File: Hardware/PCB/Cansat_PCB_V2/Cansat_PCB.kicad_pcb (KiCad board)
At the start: 6 copper layers, 31.8 x 25.4 mm, 84 parts, among them IC1 Alim STM Baro GPS IMU, IC2 Alim LoRa, J1 Lecteur SD, J2 Connecteur Batterie, J3 Connecteur STLINK, J4 Connecteur Moteur, J5 Connecteur TOF, J6 Connecteur GPS, J7 Connecteur LoRa, J9 Connecteur IHM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

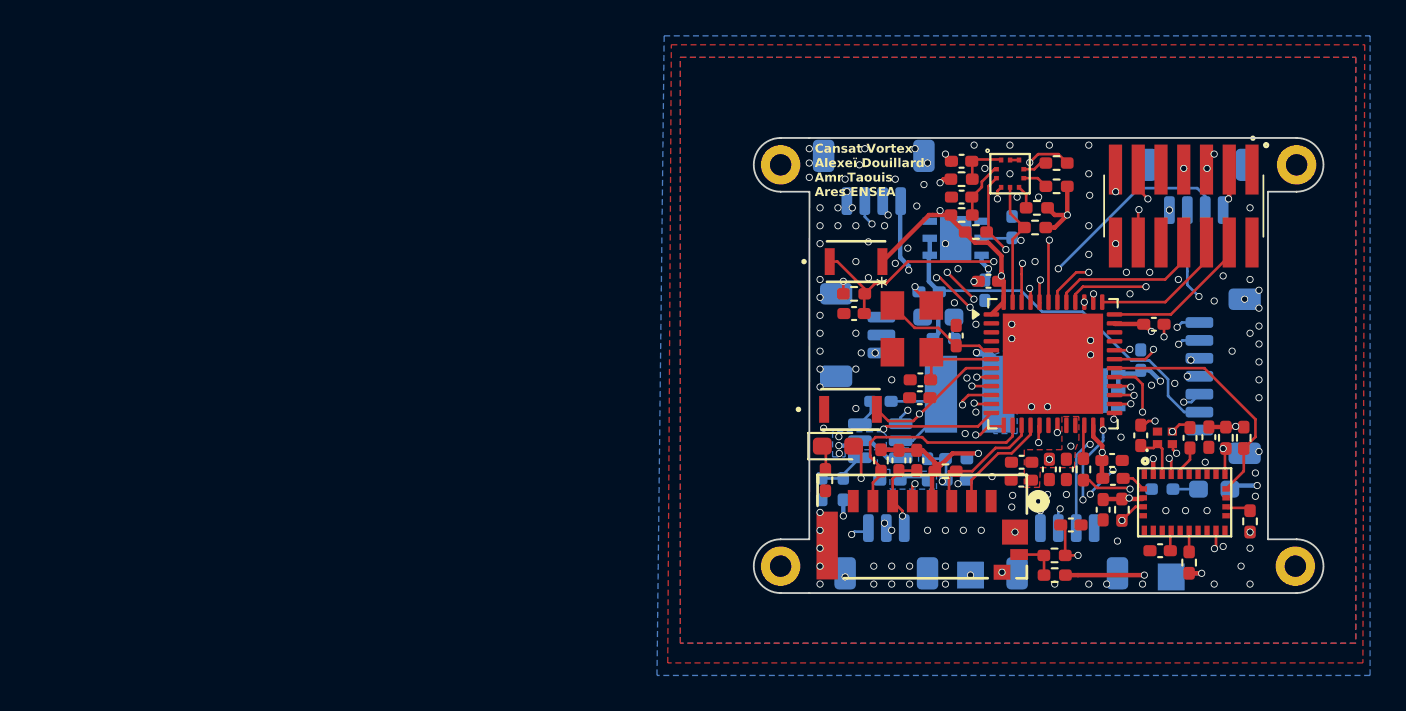
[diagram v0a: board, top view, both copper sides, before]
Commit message: ajout du connecteur IHM dans l'éditeur de PCB
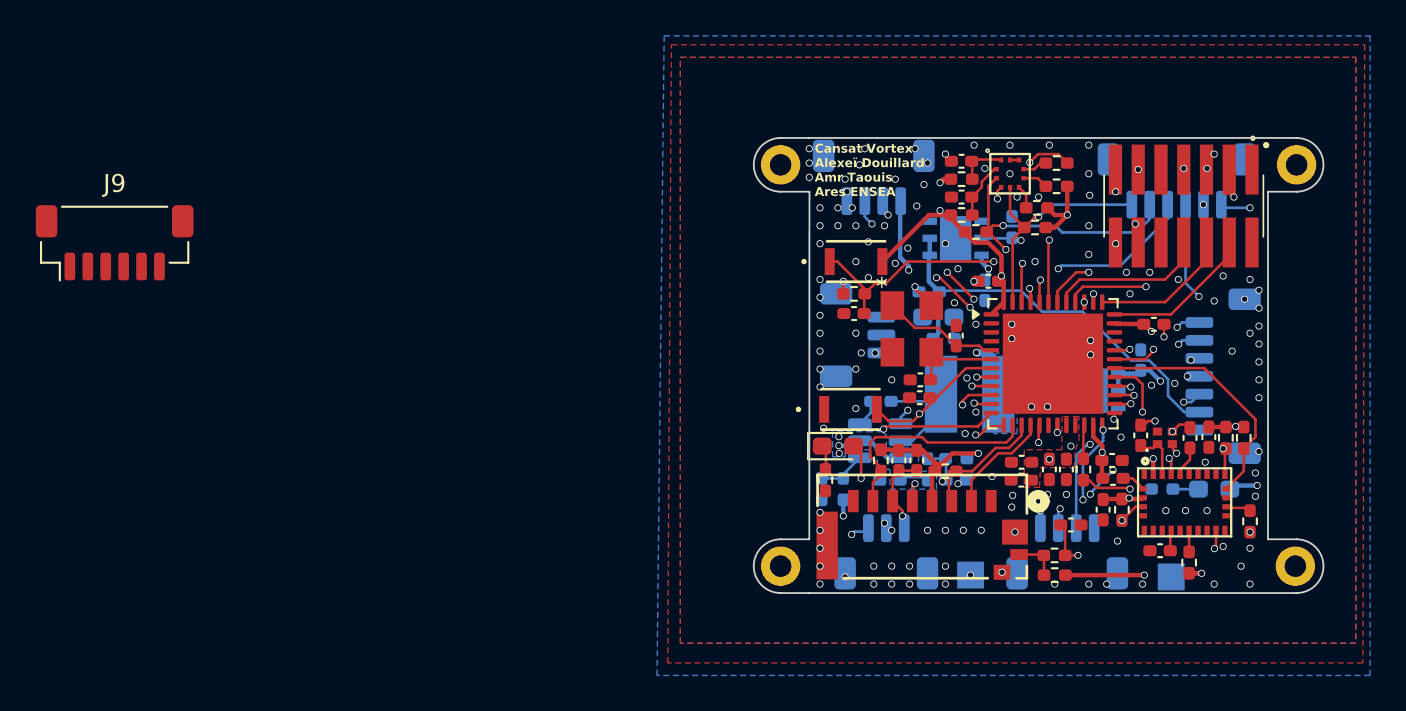
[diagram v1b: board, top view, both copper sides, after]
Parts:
- added J10: Connecteur IHM, Connector_JST:JST_SH_BM06B-SRSS-TB_1x06-1MP_P1.00mm_Vertical, B.Cu at (156.9, 90.5)
- J9: footprint Connector_JST:JST_SH_BM04B-SRSS-TB_1x04-1MP_P1.00mm_Vertical -> Connector_JST:JST_SH_BM06B-SRSS-TB_1x06-1MP_P1.00mm_Vertical; moved to F.Cu
- moved J9 60.5 mm to (97.6, 94.0), turned to 0 degrees
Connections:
- J9 pad 1: +3.3V -> GND
- J9 pad 2: EXTI3_BTN -> +3.3V
- J9 pad 3: LED_DATA -> LED_DATA_IN
- J9 pad 4: GND -> MainBTN
- J9 pad MP: GND -> (no net)
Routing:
- net I2C1_SCL: track 10.7 -> 21.2 mm, vias 2 -> 3
- net I2C1_SDA: track 7.01 -> 13.5 mm, vias 0 -> 1
- net EXTI3_BTN: track 23.9 -> 20.9 mm
- net GND: track 16.4 -> 16.2 mm, vias 142 -> 141
- net +3.3V: vias 18 -> 19

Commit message: Conn Camera 2 pins et deplacement du transistor dans un pcb intermédiaire
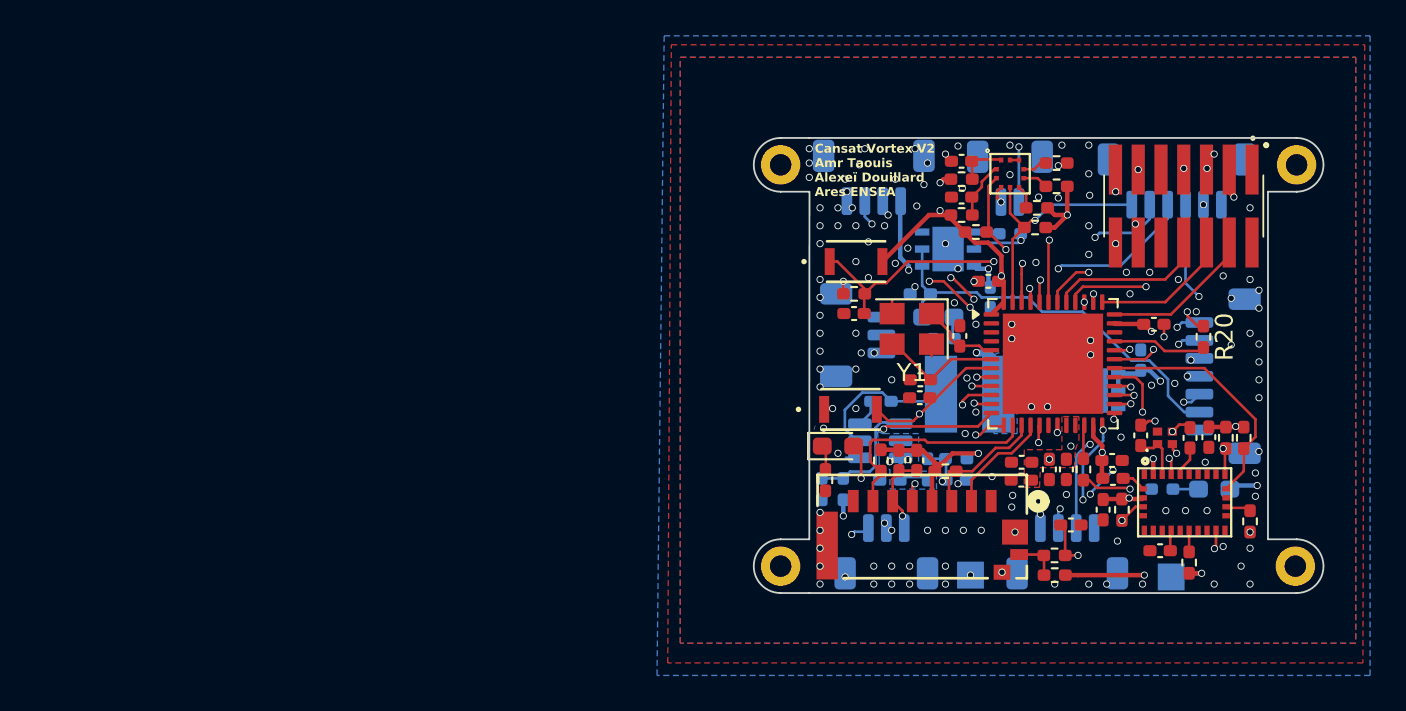
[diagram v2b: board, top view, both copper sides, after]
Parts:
- removed J9: Connecteur IHM, Connector_JST:JST_SH_BM06B-SRSS-TB_1x06-1MP_P1.00mm_Vertical
- added J8: Connecteur Camera, Connector_JST:JST_SH_BM02B-SRSS-TB_1x02-1MP_P1.00mm_Vertical, B.Cu at (147.6, 90.3)
- added R20: 10k, Resistor_SMD:R_0402_1005Metric_Pad0.72x0.64mm_HandSolder, F.Cu at (158.4, 99.2)
- Y1: footprint footprints:SMD3225_3.2X2.5X0.7_MTC -> footprints:Crystal_SMD_3225-4pin_3.2x2.5mm
- moved IC2 0.74 mm to (144.1, 94.3)
- moved C28 0.50 mm to (142.6, 96.8)
- moved C27 0.50 mm to (146.5, 97.0)
- moved R25 0.39 mm to (147.6, 93.5), turned to 180 degrees
- moved C11 0.20 mm to (144.8, 99.2)
- turned Y1 to 180 degrees
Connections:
- U2 pad 33: unconnected-(U2-PA11-Pad33) -> Net-(U2-PA11)
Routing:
- net CAM_EN: track 0.00 -> 19.9 mm, vias 0 -> 2
- net Net-(U2-PA11): track 0.00 -> 5.27 mm
- net I2C1_SCL: track 21.2 -> 17.1 mm
- net Net-(U5-FB): track 3.65 -> 7.20 mm, vias 1 -> 0
- net VIN: track 7.52 -> 5.00 mm, vias 4 -> 3
- net Net-(U5-SW): track 6.65 -> 8.75 mm
- net Net-(U2-PF0): track 6.56 -> 4.60 mm
- net Net-(U2-PF1): track 5.20 -> 6.84 mm
- net EXTI_BARO: track 27.1 -> 25.7 mm
- net PWEN: track 7.38 -> 8.31 mm
- net 3.3VEN: track 23.4 -> 22.9 mm
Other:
- board text added: "/"
- board text added: "3.3"
- board text added: "3.3 VEN"
- board text added: "5V"
- board text added: "BTN"
- board text added: "Batt"
- board text added: "Cam"
- board text added: "Cansat Vortex V2 Amr Taouis Alexeï Douillard Ares ENSEA"
- board text added: "DIO0"
- board text added: "EN"
- board text added: "GND"
- board text added: "GPS"
- board text added: "IHM"
- board text added: "LED"
- board text added: "LoRa"
- board text added: "MISO"
- board text added: "MOSI"
- board text added: "Mot"
- board text added: "NSS"
- board text added: "RX"
- board text added: "SCK"
- board text added: "SCL"
- board text added: "SDA"
- board text added: "TIM3"
- board text added: "TOF"
- board text added: "TX"
- board text added: "VIN"
- board text added: "X"
- board text removed: "Cansat Vortex Alexeï Douillard Amr Taouis Ares ENSEA"
